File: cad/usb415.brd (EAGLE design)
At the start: 45.5 x 15 mm, 40 parts, among them CN1 MICROSD-EJECT, Q1 IRLML6344TRPBF, SW2 SWITCHKMR211, SW3 SWITCHKMR211, U1 STM32F4/64, X1 12MHz, X2 USB-A

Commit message: R-array
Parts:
- removed R1, R11, R12, R3, R8, R9: (no value), jaw:SMD0603
- removed R2: 100, jaw:SMD0603
- added R13, R14: 470, jaw:SMD-0603-ARV
- moved Q1 3.50 mm to (17.0, 22.5), turned to 0 degrees
- moved LED1 3.00 mm to (13.0, 16.5)
- moved LED2 3.00 mm to (13.0, 13.5)
- moved R10 2.00 mm to (17.0, 19.5)
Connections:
- removed net N$11: LED2.CG, R12.2
- new net N$10: LED1.CG, R14.6
- net IOLED0: now also R13.2; no longer R1.1
- net IOLED1: now also R13.3; no longer R3.1
- net IOLED2: now also R13.4; no longer R8.1
- net IOLED3: now also R14.1; no longer R9.1
- net IOLED4: now also R14.2; no longer R11.1
- net IOLED5: now also R14.3; no longer R12.1
- net IOSPKR: now also R14.4; no longer R2.1
- net N$1: now also LED2.CB, R13.7; no longer LED1.CB, R1.2
- net N$2: now also LED2.CR, R13.6; no longer LED1.CR, R3.2
- net N$3: now also LED2.CG, R13.5; no longer LED1.CG, R8.2
- net N$5: now also LED1.CB, R14.8; no longer LED2.CB, R9.2
- net N$6: now also LED1.CR, R14.7; no longer LED2.CR, R11.2
- net N$9: now also R14.5; no longer R2.2
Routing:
- net N$14: track 13.4 -> 7.03 mm
- net GND: track 48.7 -> 53.0 mm
- net N$11: track 2.90 -> 0.00 mm
- net N$10: track 0.00 -> 2.24 mm
- net N$9: track 6.02 -> 3.90 mm
- net IOSPKR: track 13.6 -> 15.2 mm
- net IOLED5: track 16.4 -> 17.8 mm
- net IOLED0: track 11.6 -> 12.9 mm
- net VCC: track 60.3 -> 59.0 mm
- net IOLED4: track 9.03 -> 10.1 mm
- net IOLED1: track 11.8 -> 12.9 mm
- net N$1: track 3.10 -> 2.12 mm
- net IOLED2: track 12.0 -> 12.8 mm
- net IOLED3: track 9.45 -> 10.2 mm
- net N$2: track 2.81 -> 2.12 mm

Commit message: reverse polarity
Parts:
- turned LED1 to 0 degrees
- turned LED2 to 0 degrees
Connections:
- net GND: now also LED1.CB, LED1.CG, LED1.CR, LED2.CB, LED2.CG, LED2.CR
- net N$1: now also LED1.AG, R14.8; no longer LED2.CB, R13.7
- net N$10: now also LED2.AB, R13.5; no longer LED1.CG, R14.6
- net N$2: now also LED1.AR, R14.7; no longer LED2.CR, R13.6
- net N$3: now also LED1.AB, R14.6; no longer LED2.CG, R13.5
- net N$5: now also LED2.AG, R13.7; no longer LED1.CB, R14.8
- net N$6: now also LED2.AR, R13.6; no longer LED1.CR, R14.7
- net VCC: no longer LED1.AB, LED1.AG, LED1.AR, LED2.AB, LED2.AG, LED2.AR
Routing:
- net VCC: track 59.0 -> 50.9 mm, vias 9 -> 8
- net GND: track 53.0 -> 58.5 mm, vias 34 -> 38
- removed copper zone on layer 1, net VCC

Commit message: eeprom
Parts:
- added U2: EEPROM-I2C-8-DFN8, jaw:TDFN8
- R13, R14: value 470 -> 100
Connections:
- net GND: now also U2.1, U2.2, U2.3, U2.4, U2.7
- net I2CCL: now also U2.6
- net I2CDA: now also U2.5
- net VCC: now also U2.8
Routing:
- net I2CDA: track 0.00 -> 27.4 mm, vias 0 -> 2
- net I2CCL: track 0.00 -> 22.1 mm, vias 0 -> 2
- net GND: track 58.5 -> 66.1 mm
- net VCC: track 50.9 -> 52.2 mm, vias 8 -> 9

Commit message: tweak
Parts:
- removed LOGO2: OSHW-LOGOM, SparkFun-Aesthetics:OSHW-LOGO-M
- R13, R14: value 100 -> 470
- U2: value EEPROM-I2C-8-DFN8 -> EEPROM-I2C-8-DFN8W; device jaw:TDFN8 -> jaw:TDFN8EPW
- moved U2 0.30 mm to (20.5, 22.7), turned to 270 degrees
- moved D1 0.20 mm to (13.0, 19.2)
- moved LED1 0.20 mm to (13.0, 16.7)
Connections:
- net GND: now also U2.PAD
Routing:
- net GND: track 66.1 -> 69.4 mm
- net VCC: track 52.2 -> 51.5 mm

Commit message: tweak
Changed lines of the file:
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@@
 <wire x1="20.75" y1="21.3" x2="20.75" y2="23.2" width="0.25" layer="1"/>
 <wire x1="20.75" y1="23.2" x2="21.1" y2="23.2" width="0.25" layer="1"/>
+<contactref element="U2" pad="PAD"/>
 <wire x1="49" y1="14" x2="47.7" y2="14" width="0" layer="19" extent="1-1"/>
 <wire x1="38.8" y1="18.8" x2="40.5" y2="19" width="0" layer="19" extent="1-1"/>
 <wire x1="36.5" y1="22.9" x2="34.75" y2="23.1" width="0" layer="19" extent="1-1"/>
 <wire x1="22" y1="10.8" x2="25.3" y2="11" width="0" layer="19" extent="1-1"/>
-<contactref element="U2" pad="PAD"/>
 </signal>
 <signal name="VCC">
@@
 <contactref element="VR1" pad="3"/>
 <via x="47.5" y="10.9" extent="1-16" drill="0.5"/>
-<via x="51" y="22.3" extent="1-16" drill="0.5"/>
+<via x="50.5" y="22.4" extent="1-16" drill="0.5"/>
 <wire x1="47.5" y1="10.9" x2="48.3" y2="10.9" width="0.5" layer="16"/>
-<wire x1="48.3" y1="10.9" x2="51" y2="13.6" width="0.5" layer="16"/>
-<wire x1="51" y1="13.6" x2="51" y2="19.2" width="0.5" layer="16"/>
+<wire x1="48.3" y1="10.9" x2="50.5" y2="13.1" width="0.5" layer="16"/>
+<wire x1="50.5" y1="13.1" x2="50.5" y2="19.2" width="0.5" layer="16"/>
 <wire x1="49" y1="11.2" x2="47.8" y2="11.2" width="0.5" layer="1"/>
 <wire x1="47.8" y1="11.2" x2="47.5" y2="10.9" width="0.5" layer="1"/>
@@
 <wire x1="47.5" y1="11.6" x2="47.5" y2="10.9" width="0.5" layer="1"/>
 <contactref element="X2" pad="1"/>
-<wire x1="51" y1="19.2" x2="51" y2="22.3" width="0.5" layer="16"/>
-<wire x1="50.9" y1="21" x2="51" y2="21.1" width="0.5" layer="1"/>
-<wire x1="51" y1="21.1" x2="51" y2="22.3" width="0.5" layer="1"/>
+<wire x1="50.5" y1="19.2" x2="50.5" y2="22.4" width="0.5" layer="16"/>
+<wire x1="50.9" y1="21" x2="50.5" y2="21" width="0.5" layer="1"/>
+<wire x1="50.5" y1="21" x2="50.5" y2="22.4" width="0.5" layer="1"/>
 </signal>
 <signal name="I2CCL">
@@
 <contactref element="R10" pad="1"/>
 <contactref element="R14" pad="5"/>
-<wire x1="15.875" y1="17.7" x2="15.875" y2="18.475" width="0.25" layer="1"/>
-<wire x1="15.875" y1="18.475" x2="16.2" y2="18.8" width="0.25" layer="1"/>
 <wire x1="16.2" y1="18.8" x2="16.2" y2="19.5" width="0.25" layer="1"/>
 <wire x1="16.2" y1="19.5" x2="16.2" y2="21.25" width="0.25" layer="1"/>
 <wire x1="16.2" y1="21.25" x2="16.05" y2="21.4" width="0.25" layer="1"/>
+<wire x1="15.8" y1="17.7" x2="15.8" y2="18.4" width="0.25" layer="1"/>
+<wire x1="15.8" y1="18.4" x2="16.2" y2="18.8" width="0.25" layer="1"/>
 </signal>
 <signal name="SDIOD0">
@@
 <wire x1="22.3" y1="12.4" x2="20.9" y2="11" width="0.25" layer="1"/>
 <contactref element="R13" pad="2"/>
-<wire x1="17.125" y1="12.6" x2="17.8" y2="12.6" width="0.25" layer="1"/>
+<wire x1="17.2" y1="12.6" x2="17.8" y2="12.6" width="0.25" layer="1"/>
 <wire x1="17.8" y1="12.6" x2="19.4" y2="11" width="0.25" layer="1"/>
 <wire x1="19.4" y1="11" x2="20.9" y2="11" width="0.25" layer="1"/>
@@
 <wire x1="20.7" y1="11.7" x2="19.6" y2="11.7" width="0.25" layer="1"/>
 <contactref element="R13" pad="3"/>
-<wire x1="17.125" y1="13.4" x2="17.9" y2="13.4" width="0.25" layer="1"/>
+<wire x1="17.2" y1="13.4" x2="17.9" y2="13.4" width="0.25" layer="1"/>
 <wire x1="17.9" y1="13.4" x2="19.6" y2="11.7" width="0.25" layer="1"/>
 </signal>
@@
 <wire x1="20.5" y1="12.4" x2="19.8" y2="12.4" width="0.25" layer="1"/>
 <contactref element="R13" pad="4"/>
-<wire x1="17.125" y1="14.2" x2="18" y2="14.2" width="0.25" layer="1"/>
+<wire x1="17.2" y1="14.2" x2="18" y2="14.2" width="0.25" layer="1"/>
 </signal>
 <signal name="IOSPKR">
@@
 <via x="23.5" y="20" extent="1-16" drill="0.35"/>
 <contactref element="R14" pad="4"/>
-<wire x1="17.125" y1="17.7" x2="17.6" y2="17.7" width="0.25" layer="1"/>
+<wire x1="17.2" y1="17.7" x2="17.6" y2="17.7" width="0.25" layer="1"/>
 <wire x1="17.6" y1="17.7" x2="19.7" y2="19.8" width="0.25" layer="1"/>
 <wire x1="19.7" y1="19.8" x2="23.3" y2="19.8" width="0.25" layer="1"/>
@@
 <wire x1="21.85" y1="18.75" x2="18.6" y2="15.5" width="0.25" layer="1"/>
 <contactref element="R14" pad="1"/>
-<wire x1="17.125" y1="15.3" x2="18.4" y2="15.3" width="0.25" layer="1"/>
+<wire x1="17.2" y1="15.3" x2="18.4" y2="15.3" width="0.25" layer="1"/>
 <wire x1="18.4" y1="15.3" x2="18.6" y2="15.5" width="0.25" layer="1"/>
 </signal>
@@
 <wire x1="21.35" y1="19.25" x2="19.1" y2="17" width="0.25" layer="1"/>
 <contactref element="R14" pad="2"/>
-<wire x1="17.125" y1="16.1" x2="18.2" y2="16.1" width="0.25" layer="1"/>
+<wire x1="17.2" y1="16.1" x2="18.2" y2="16.1" width="0.25" layer="1"/>
 <wire x1="18.2" y1="16.1" x2="19.1" y2="17" width="0.25" layer="1"/>
 </signal>
@@
 <via x="30.8" y="20.1" extent="1-16" drill="0.35"/>
 <contactref element="R14" pad="3"/>
-<wire x1="17.125" y1="16.9" x2="17.8" y2="16.9" width="0.25" layer="1"/>
+<wire x1="17.2" y1="16.9" x2="17.8" y2="16.9" width="0.25" layer="1"/>
 <wire x1="17.8" y1="16.9" x2="19.4" y2="18.5" width="0.25" layer="1"/>
 </signal>
@@
 <wire x1="13.9" y1="15.9" x2="14.6" y2="15.9" width="0.25" layer="1"/>
 <wire x1="14.6" y1="15.9" x2="15.2" y2="15.3" width="0.25" layer="1"/>
-<wire x1="15.2" y1="15.3" x2="15.875" y2="15.3" width="0.25" layer="1"/>
+<wire x1="15.2" y1="15.3" x2="15.8" y2="15.3" width="0.25" layer="1"/>
 </signal>
 <signal name="N$2">
@@
 <wire x1="13.9" y1="16.7" x2="14.6" y2="16.7" width="0.25" layer="1"/>
 <wire x1="14.6" y1="16.7" x2="15.2" y2="16.1" width="0.25" layer="1"/>
-<wire x1="15.2" y1="16.1" x2="15.875" y2="16.1" width="0.25" layer="1"/>
+<wire x1="15.2" y1="16.1" x2="15.8" y2="16.1" width="0.25" layer="1"/>
 </signal>
 <signal name="N$3">
@@
 <wire x1="13.9" y1="17.5" x2="14.6" y2="17.5" width="0.25" layer="1"/>
 <wire x1="14.6" y1="17.5" x2="15.2" y2="16.9" width="0.25" layer="1"/>
-<wire x1="15.2" y1="16.9" x2="15.875" y2="16.9" width="0.25" layer="1"/>
+<wire x1="15.2" y1="16.9" x2="15.8" y2="16.9" width="0.25" layer="1"/>
 </signal>
 <signal name="N$5">
@@
 <wire x1="13.9" y1="12.7" x2="15" y2="12.7" width="0.25" layer="1"/>
 <wire x1="15" y1="12.7" x2="15.1" y2="12.6" width="0.25" layer="1"/>
-<wire x1="15.1" y1="12.6" x2="15.875" y2="12.6" width="0.25" layer="1"/>
+<wire x1="15.1" y1="12.6" x2="15.8" y2="12.6" width="0.25" layer="1"/>
 </signal>
 <signal name="N$6">
@@
 <wire x1="13.9" y1="13.5" x2="15.1" y2="13.5" width="0.25" layer="1"/>
 <wire x1="15.1" y1="13.5" x2="15.2" y2="13.4" width="0.25" layer="1"/>
-<wire x1="15.2" y1="13.4" x2="15.875" y2="13.4" width="0.25" layer="1"/>
+<wire x1="15.2" y1="13.4" x2="15.8" y2="13.4" width="0.25" layer="1"/>
 </signal>
 <signal name="N$10">
@@
 <wire x1="13.9" y1="14.3" x2="15.1" y2="14.3" width="0.25" layer="1"/>
 <wire x1="15.1" y1="14.3" x2="15.2" y2="14.2" width="0.25" layer="1"/>
-<wire x1="15.2" y1="14.2" x2="15.875" y2="14.2" width="0.25" layer="1"/>
+<wire x1="15.2" y1="14.2" x2="15.8" y2="14.2" width="0.25" layer="1"/>
 </signal>
 </signals>

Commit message: sd connector
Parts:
- removed C21: .1u, jaw:SMD0603
- removed C22: 4u7, jaw:SMD0603
- removed R10: 1M, jaw:SMD0603
- removed R13, R14: 470, jaw:SMD-0603-ARV
- removed SW3: SWITCHKMR211, jaw:KMR211
- added C5, C6: 2u2, jaw:SMD0603
- added R1, R2: 10k, jaw:SMD0603
- added R3: 22, jaw:SMD0603
- added SW1: SWITCHKMR211, jaw:KMR211
- C10: value 2u2 -> .1u
- C11: value 10u -> 4u7
- C3: value 4u7 -> 10u
- C4: value 2u2 -> 4u7
- CN1: value MICROSD-EJECT -> MICROSDPLAIN; device jaw:MICROSD/EJECTOR -> jaw:MICROSD/MOLEX/FRONT/PLAIN
- R4: value 10k -> 22
- R5: value 10k -> 1M
- R6, R7: value 22 -> 470; device jaw:SMD0603 -> jaw:SMD-0603-ARV
- moved R6 31.3 mm to (16.5, 13.0), turned to 90 degrees
- moved R7 31.0 mm to (16.5, 16.5), turned to 90 degrees
- moved C3 28.5 mm to (41.5, 12.0), turned to 90 degrees
- moved R5 27.1 mm to (17.0, 19.5), turned to 0 degrees
- moved C10 18.7 mm to (38.0, 11.0), turned to 0 degrees
- moved C11 17.0 mm to (24.5, 12.5), turned to 0 degrees
- moved C4 11.5 mm to (13.0, 11.0)
- moved R4 7.07 mm to (47.5, 17.0), turned to 180 degrees
- moved SW2 3.00 mm to (45.0, 21.0)
- moved CN1 0.71 mm to (19.5, 17.0)
- renumbered C15 to C7, C19 to C8, C20 to C9, C23 to C12, SPKR2 to SPKR1
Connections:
- net BOOT0: now also R1.2, SW2.2, SW2.4; no longer R4.2, SW3.2, SW3.4
- net GND: now also C5.2, C6.2, CN1.SW2, R1.1, R5.2, SW1.1, SW1.3; no longer C21.2, C22.2, CN1.SHELL1, R10.2, R4.1, SW2.1, SW2.3
- net IOCARD: now also CN1.SW1; no longer CN1.CD1
- net IOLED0: now also R6.2; no longer R13.2
- net IOLED1: now also R6.3; no longer R13.3
- net IOLED2: now also R6.4; no longer R13.4
- net IOLED3: now also R7.1; no longer R14.1
- net IOLED4: now also R7.2; no longer R14.2
- net IOLED5: now also R7.3; no longer R14.3
- net IOSPKR: now also R7.4; no longer R14.4
- net N$1: now also R7.8; no longer R14.8
- net N$10: now also R6.5; no longer R13.5
- net N$18: now also C5.1; no longer C10.1
- net N$2: now also R7.7; no longer R14.7
- net N$3: now also R7.6; no longer R14.6
- net N$4: now also C6.1; no longer C4.1
- net N$5: now also R6.7; no longer R13.7
- net N$6: now also R6.6; no longer R13.6
- net N$7: now also R4.1; no longer R6.1
- net N$8: now also R3.1; no longer R7.1
- net N$9: now also R5.1, R7.5; no longer R10.1, R14.5
- net NRST: now also R2.1, SW1.2, SW1.4; no longer R5.1, SW2.2, SW2.4
- net USBDM: now also R4.2; no longer R6.2
- net USBDP: now also R3.2; no longer R7.2
- net VCC: now also C10.1, C4.1, R2.2, SW2.1, SW2.3; no longer C21.1, C22.1, R5.2, SW3.1, SW3.3
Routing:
- net IOCARD: track 3.02 -> 28.0 mm, vias 1 -> 3
- net VCC: track 51.5 -> 53.3 mm, vias 9 -> 10
- net SDIOD3: track 20.3 -> 21.9 mm
- net SDIOCMD: track 20.8 -> 22.1 mm
- net SDIOD2: track 20.7 -> 21.8 mm
- net SDIOCLK: track 16.9 -> 17.9 mm
- net IOLED5: track 17.9 -> 18.9 mm
- net IOSPKR: track 15.2 -> 15.9 mm
- net I2CDA: track 27.2 -> 27.9 mm
- net GND: track 69.4 -> 70.0 mm, vias 38 -> 40
- net SDIOD1: track 13.6 -> 14.1 mm
- net SDIOD0: track 13.2 -> 13.7 mm
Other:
- outline, holes or cut-outs redrawn

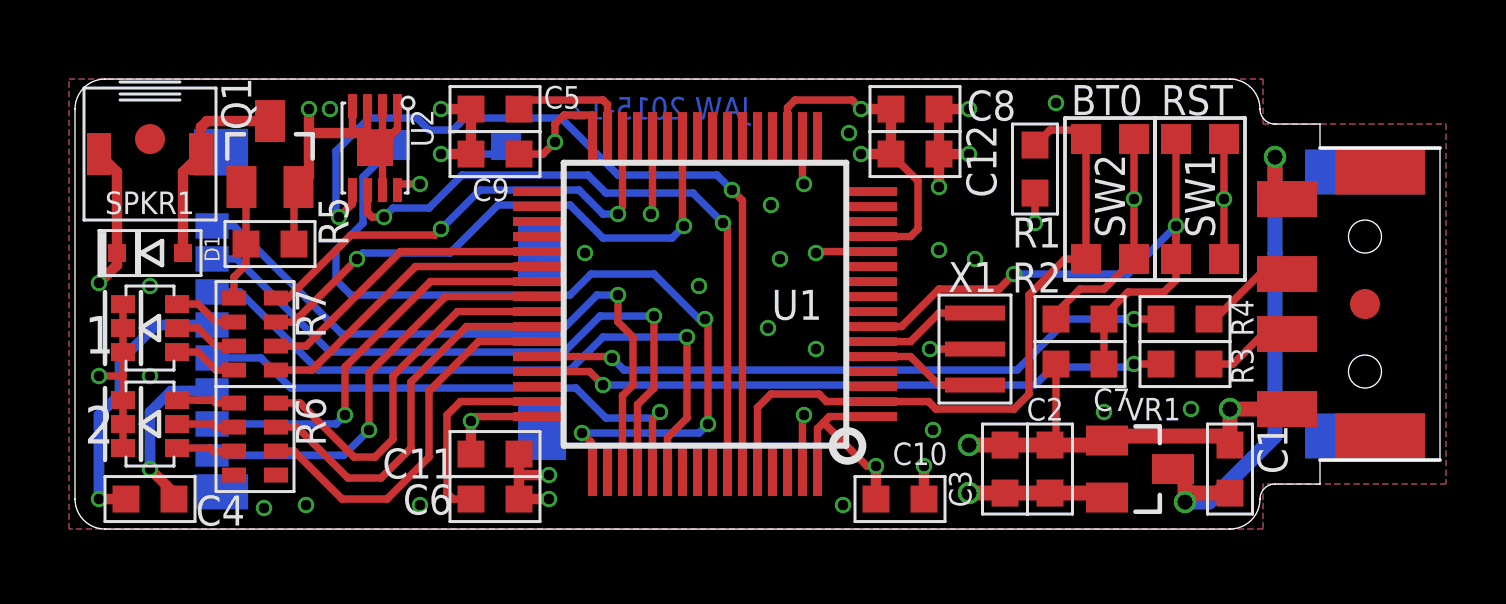
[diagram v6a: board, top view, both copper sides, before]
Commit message: add prog/test header
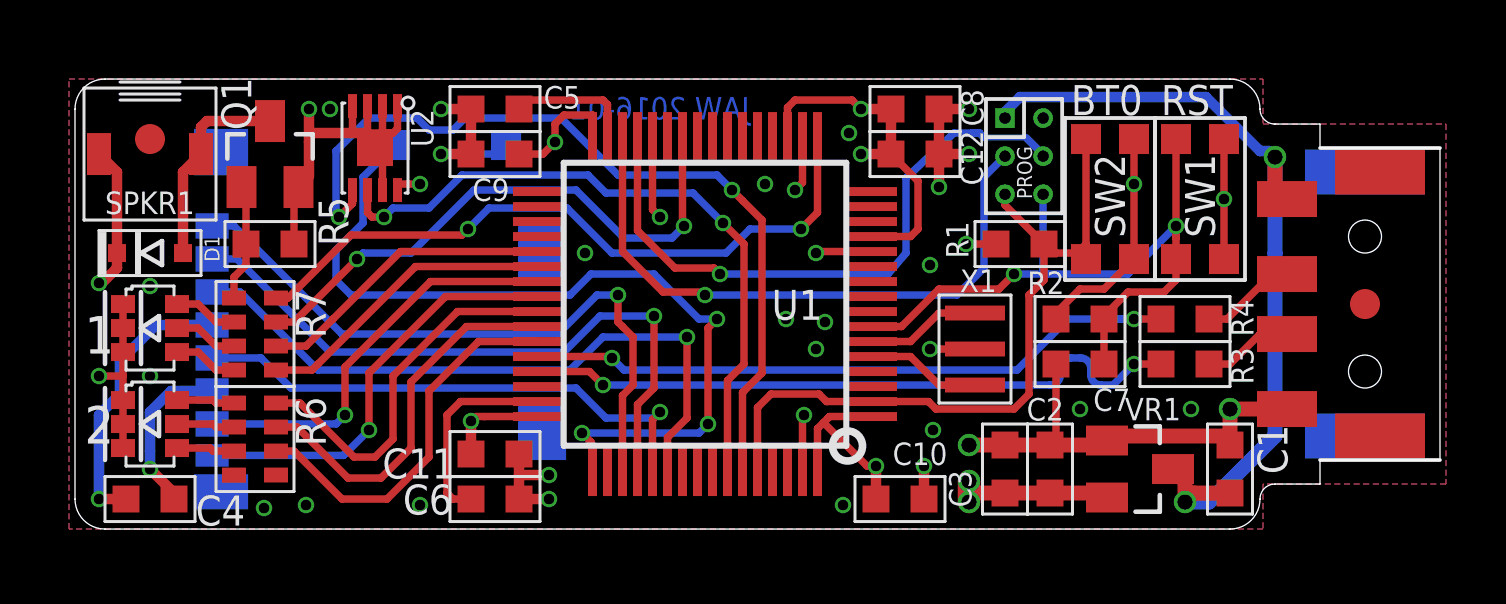
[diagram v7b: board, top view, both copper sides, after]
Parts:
- added CN2: HEADER-3X2-PTH1.27, jaw:HEADER-3X2-PTH1.27
- moved R1 2.55 mm to (42.0, 19.5), turned to 0 degrees
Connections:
- new net RX: CN2.3, U1.30
- new net TX: CN2.4, U1.29
- net BOOT0: now also CN2.5
- net GND: now also CN2.2
- net IOSPKR: now also U1.17; no longer U1.30
- net NRST: now also CN2.6
- net VUSB: now also CN2.1
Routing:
- net TX: track 0.00 -> 21.6 mm, vias 0 -> 1
- net RX: track 0.00 -> 20.9 mm, vias 0 -> 1
- net VUSB: track 17.9 -> 28.1 mm
- net IOSPKR: track 15.9 -> 23.0 mm
- net NRST: track 21.1 -> 23.8 mm
- net BOOT0: track 23.5 -> 25.4 mm
- net VCC: track 53.3 -> 54.4 mm, vias 10 -> 11
- net USBDP: track 21.3 -> 22.3 mm
- net N$7: track 2.32 -> 3.22 mm
- net N$8: track 2.21 -> 3.01 mm
- net I2CCL: track 22.3 -> 22.9 mm
- net I2CDA: track 27.9 -> 28.4 mm
- net GND: track 70.0 -> 70.4 mm, vias 40 -> 37
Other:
- board text added: "JAW 2016-01"
- board text added: "PROG"
- board text added: "usb415 Rev. 1"
- board text removed: "JAW 2015-12"
- board text removed: "usb/sd Rev. 0"
